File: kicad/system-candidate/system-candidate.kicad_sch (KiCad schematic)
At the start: 204 parts, among them J1 691137710002 2P 5.00mm, J2 Auxiliary 12V, J3 Differential audio, J301 T1_SECONDARY, J4 Control 2x4: 3V3 RESET FAULT 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, J401 START_BUTTON, J5 691137710002 2P 5.00mm, J6 GND braid solder bond - NO mo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, K501 G6K-2F DC12, Q501 MMBT3904, Q502 MMBT3904, U1 TPA3255DDV, U2 OPA1656ID, U3 OPA1656ID, U302 LM5164DDA, U303 TPS3700DDC, U401 LP2985-33, U402 TPS3808G33, U403 TPS3808G33, U404 TPS3808G33, U405 74LVC1G14, U406 74LVC2G74, U407 74LVC2G74, U408 74LVC1G32, U409 74LVC1G07, U410 74LVC1G08, U411 74LVC1G06, U412 TPS3700DDC, U413 TPS3700DDC, U414 TPS3808G33, U415 74LVC1G08, U416 TPS3808G33, U417 74LVC2G74, U418 74LVC1G32, U419 74LVC1G07, U501 TPS3700DDC, U502 TPS3700DDC, U503 TMUX6219, U504 TPS3700DDC

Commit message: feat(pcb): placa única D-030 com potência fechada e regras pragmáticas
- revoga D-029 (Rev A/Rev B) e remove kicad/rev-a-bench
- J301 JST B3P-VH (manual PS28 p.14), D301/D302 P600J, C301/C302 em footprint D30,
  F301 Littelfuse 02186.3MXP; R201 DIN0617 vertical
- ERC: pinos PBTL paralelos passive e TP101 MONO_IN (de fix/pcb-route-drc-erc)
- system-candidate regenerada: 205 footprints, ERC 0, DRC 0, paridade 0,
  471 conexões para rota manual; autoroute de estudo descartado; galeria 3D refeita
- AGENTS.md/safety/PLANNING: política de evidência pragmática e Done objetivo
- tasks SETUP-003, PCB-003, PWR-001, ELEC-001 e SYS-001 concluídas
- roteiro de medidas restantes em mechanical/measurement-request.md
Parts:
- added TP101: MONO_IN, TestPoint:TestPoint_Pad_D2.0mm, symbol Connector:TestPoint
- C301, C302: footprint Capacitor_THT:CP_Radial_D25.0mm_P10.00mm_SnapIn -> Capacitor_THT:CP_Radial_D30.0mm_P10.00mm_SnapIn; MPN Rubycon 63USC4700MEFCSN30X30 (LCSC C1498587): 4700 uF/63 V, 3.49 A rms @120 Hz, D30xL30, 3000 h @85 C (D-025) -> Rubycon 63USC4700MEFCSN30X30 (LCSC C1498587): 4700 uF/63 V, 3.49 A rms @120 Hz, D30xL30; with C14/C15 3000 uF >= OEM 2x6800 uF/50 V margin on voltage (D-030)
- D301, D302: value MUR3040WTG -> P600J; MPN onsemi MUR3040WTG (MUR3020WT/D Rev.7): VRRM 400 V, IF(AV) 1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 -> P600J (Diodes Inc./Vishay), R-6 axial: 600 V, 6 A, IFSM 400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
- F301: MPN Time-lag (T) 5x20 mm; I2t melt above measured inrush, >=63 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 -> Littelfuse 02186.3MXP, 218 series T 6.3 A 5x20 mm, in Schur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
- J301: MPN JST VH SVH-41T-P1.1 terminals (20-16 AWG, 10 A) on VHR-4N h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 -> JST B3P-VH(LF)(SN) header 3 pos 3.96 mm; mates OEM T1 harne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
- R201: footprint Resistor_THT:R_Axial_DIN0617_L17.0mm_D6.0mm_P20.32mm_Horizontal -> Resistor_THT:R_Axial_DIN0617_L17.0mm_D6.0mm_P5.08mm_Vertical
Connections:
- net MONO_BIASED: now also TP101.1

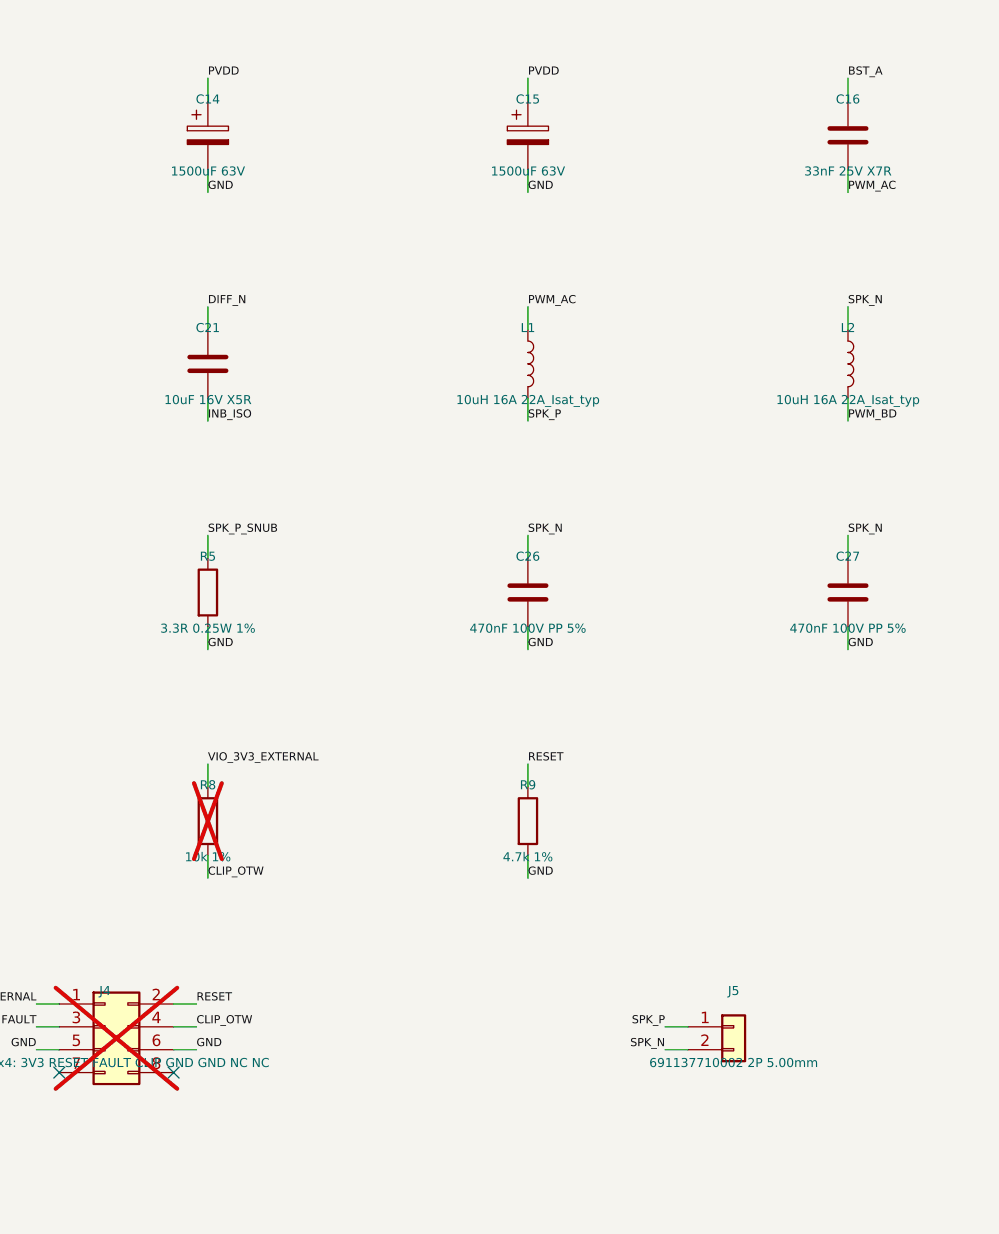
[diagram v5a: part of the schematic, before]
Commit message: feat(pcb): bloco térmico do TPA3255, J5 VH e medidas finais (D-031)
- medidas do proprietário: furos M3 roscados no perfil, perfil flutuante,
  polaridade do woofer e resistências de T1 (CT no pino central)
- placer: keepout do bloco térmico (só SMD baixo sob o bloco), J6 para trança GND
- J5 -> JST B2P-VH (chicote original do woofer); C14/C15 -> UHE1J681MHD D12,5,
  bulk PVDD 10,76 mF
- system-candidate regenerada: ERC 0, DRC 0, paridade 0, 471 conexões a rotear
- MECH-001 concluída; PCB-001 em andamento; gabarito 1:1 movido para FAB-001
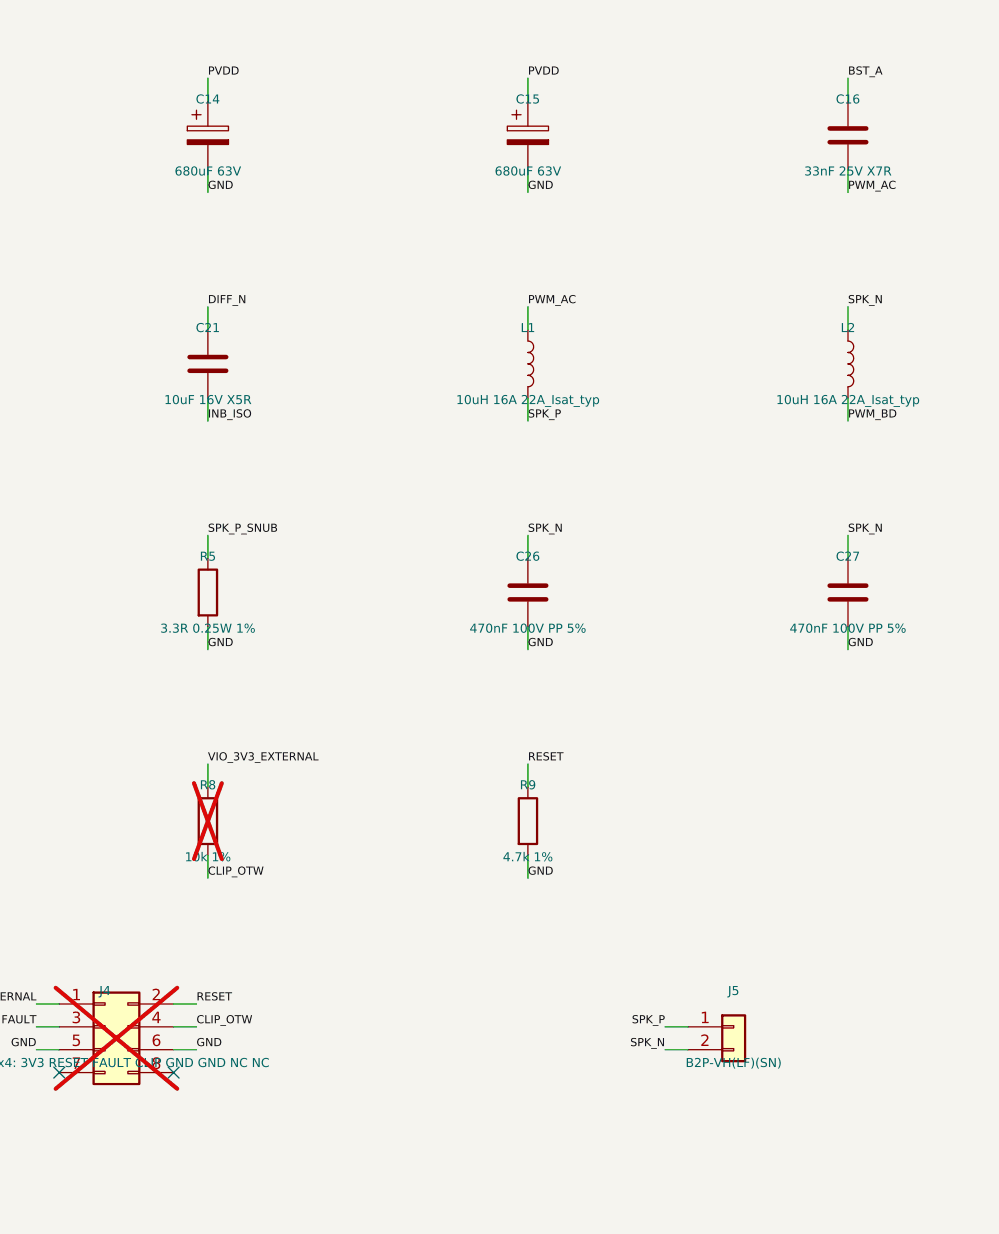
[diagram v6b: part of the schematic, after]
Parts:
- C14, C15: value 1500uF 63V -> 680uF 63V; footprint Capacitor_THT:CP_Radial_D18.0mm_P7.50mm -> Capacitor_THT:CP_Radial_D12.5mm_P5.00mm
- J5: value 691137710002 2P 5.00mm -> B2P-VH(LF)(SN); footprint PS28:WE_WR_TBL_691137710002 -> Connector_JST:JST_VH_B2P-VH_1x02_P3.96mm_Vertical

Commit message: feat(pcb): front-end OEM, placement final, bloco térmico e rota com planos
- D-032: preamp/limiter originais via J7 (JST XH 7 vias), ±15 V discretos,
  LIMIT por CLIP_OTW, ganho U2A 1,887; LR4 onboard removido
- placement revisado: LC junto do U1, buck sob L301, retificador do lado de T1
- bloco térmico: cotas, STL e modelo 3D (Blender); H5/H6 M3 em GND
- J5: modelo 3D JST B2P-VH feito no Blender
- cobre: planos GND/PVDD, fills, fanout do U1; 2.343 trilhas, 310 vias
- ERC 0, paridade 0; 56 conexões abertas e 4 starved_thermal pendentes
- ELEC-002/ELEC-004 concluídas; PCB-002 em andamento; nova task PCB-004
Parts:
- removed C101, C102, C103, C104, C105, C106: 100n, Capacitor_THT:C_Rect_L7.2mm_W5.0mm_P5.00mm, symbol Device:C
- removed R103, R104, R105, R106: 14k, Resistor_SMD:R_0805_2012Metric, symbol Device:R
- removed TP101: MONO_IN, TestPoint:TestPoint_Pad_D2.0mm, symbol Connector:TestPoint
- added C109: 2.2u 63V film, Capacitor_THT:C_Rect_L7.2mm_W5.5mm_P5.00mm_FKS2_FKP2_MKS2_MKP2, symbol Device:C
- added C601, C604: 10u 25V, Capacitor_SMD:C_1206_3216Metric, symbol Device:C
- added C602, C605: 100n, Capacitor_SMD:C_0603_1608Metric, symbol Device:C
- added C603: 120u 63V, Capacitor_THT:CP_Radial_D8.0mm_P3.50mm, symbol Device:C_Polarized
- added D601, D604: BZT52C16, Diode_SMD:D_SOD-123, symbol Device:D_Zener
- added D602, D603: S1M, Diode_SMD:D_SMA, symbol Device:D
- added J7: B7B-XH-A(LF)(SN), Connector_JST:JST_XH_B7B-XH-A_1x07_P2.50mm_Vertical, symbol Connector_Generic:Conn_01x07
- added Q601: BCP56, Package_TO_SOT_SMD:SOT-223-3_TabPin2, symbol PS28_PRE:BCP56
- added Q602: BCP53, Package_TO_SOT_SMD:SOT-223-3_TabPin2, symbol PS28_PRE:BCP53
- added Q603: BSS138, Package_TO_SOT_SMD:SOT-23, symbol PS28_PRE:BSS138
- added R110: 8.87k, Resistor_SMD:R_0603_1608Metric, symbol Device:R
- added R111, R605: 10k, Resistor_SMD:R_0603_1608Metric, symbol Device:R
- added R601, R603: 470 1W, Resistor_SMD:R_2512_6332Metric, symbol Device:R
- added R602, R604: 10k, Resistor_SMD:R_1206_3216Metric, symbol Device:R
- added TP102: STB, TestPoint:TestPoint_Pad_D2.0mm, symbol Connector:TestPoint
- added TP103: PTC, TestPoint:TestPoint_Pad_D2.0mm, symbol Connector:TestPoint
- R101: value 10k -> 1k; MPN TBD -> CRCW06031K00FKEA
- R102: value 10k -> 100k; MPN TBD -> CRCW0603100KFKEA
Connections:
- net Y1 is gone; now on net VMID: U2.5 (+)
- net Y2 is gone; now on net BUFFERED: U3.3 (+)
- net BUFFERED: now also R110.1; no longer U2.2 (-)
- net CLIP_OTW: now also Q603.1 (G)
- net GND: now also C601.2, C602.2, C603.1, C604.1, C605.1, D601.2 (A), D604.1 (K), J7.4 (Pin_4), Q603.2 (S)
- net MONO_BIASED: now also C109.2
- net PVDD: now also R601.1, R602.1
- net T1_A: now also D602.1 (K)
- net T1_B: now also D603.1 (K)
- net VMID: now also R111.2
- net FILTERED1 renamed U2B_PARK
- new net LIMIT: J7.1 (Pin_1), Q603.3 (D), R605.2
- new net N15V: C604.2, J7.3 (Pin_3), Q602.3 (E)
- new net N15_BASE: C605.2, D604.2 (A), Q602.1 (B), R604.2
- new net N15_COL: Q602.2 (C), R603.2
- new net NRAW: C603.2, D602.2 (A), D603.2 (A), R603.1, R604.1
- new net P15V: C601.1, J7.5 (Pin_5), Q601.3 (E), R605.1
- new net P15_BASE: C602.1, D601.1 (K), Q601.1 (B), R602.2
- new net P15_COL: Q601.2 (C), R601.2
- new net PRE_IN: C109.1, J7.7 (Pin_7)
- new net PTC: J7.6 (Pin_6), TP103.1
- new net STB: J7.2 (Pin_2), TP102.1
- new net U2_FB: R110.2, R111.1, U2.2 (-)
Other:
- note added: "D-032 OEM PREAMP/LIMITER INTERFACE: P101, +/-15 V, LIMIT FROM CLIP_OTW"
